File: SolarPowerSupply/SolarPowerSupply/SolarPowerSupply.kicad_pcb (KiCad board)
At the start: 2 copper layers, 43 x 26.4 mm, 16 parts, among them J1 Conn_01x02_Pin, J2 Conn_01x02_Pin, J3 Conn_01x02_Pin, J4 Conn_01x02_Pin, Q1 2N7002, U1 AP3015AKTR-G1

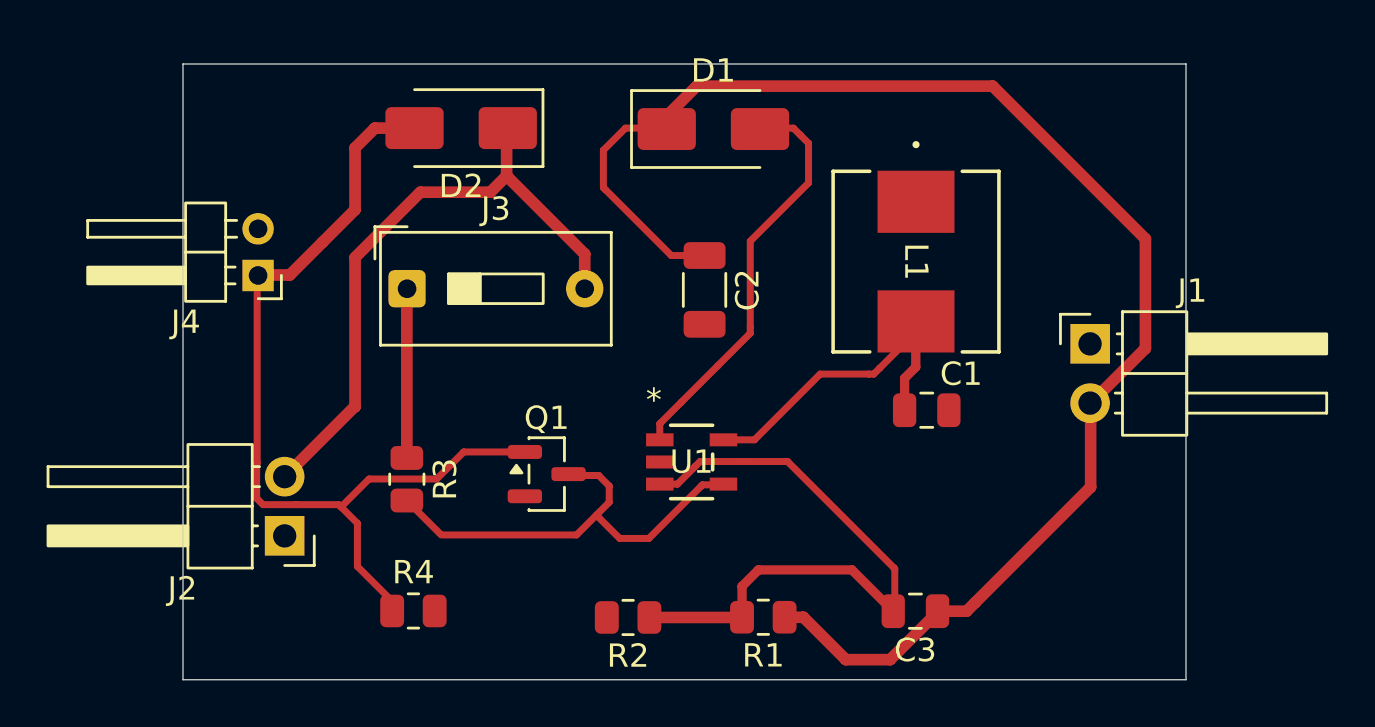
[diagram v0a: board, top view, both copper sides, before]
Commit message: Finished solar power
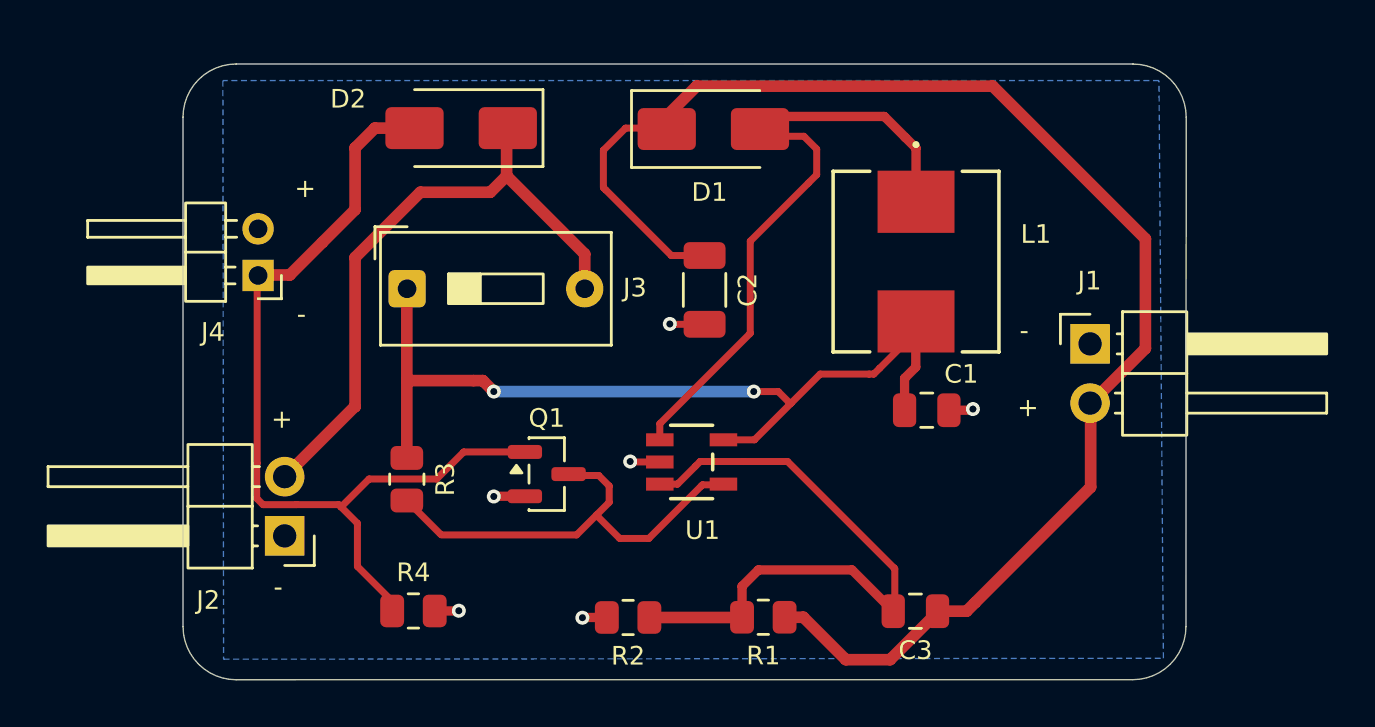
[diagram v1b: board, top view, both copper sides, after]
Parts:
- added REF**: KiCad-Logo2_5mm_SilkScreen, Symbol:KiCad-Logo2_5mm_SilkScreen, B.Cu at (205.9, 72.3)
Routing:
- net Net-(J3-Pin_1): track 21.1 -> 37.9 mm, vias 0 -> 2
- net Net-(D1-A): track 17.7 -> 27.3 mm
- net GNDD: track 0.00 -> 7.25 mm, vias 0 -> 6
- added copper zone on B.Cu, net GNDD
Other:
- outline, holes or cut-outs redrawn
- board text added: "+"
- board text added: "-"
- board text added: "Version 1.0 Mini Solar Power Supply Created by Clemens Valens for Elektor Copied by Björn Olsson for training purposes"
